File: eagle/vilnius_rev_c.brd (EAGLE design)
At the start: 72 x 42 mm, 43 parts, among them IC1 PIC18F2580, IC3 MCP2551SN, IC4 LM2575S, IC5 MCP604, J1 OSTTE-12, J2 A00-108-220-450, Q1 10 MHz

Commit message: Main functionality in place
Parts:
- moved R107 0.14 mm to (9.67, 30.6)
- moved R102 0.14 mm to (9.64, 13.1)
- moved R101 0.10 mm to (9.61, 9.64)
- moved R103 0.10 mm to (9.61, 16.7)
- moved R105 0.10 mm to (9.62, 23.7)
- moved R100 0.10 mm to (9.59, 6.15)
- moved R104 0.10 mm to (9.59, 20.1)
- moved R106 0.10 mm to (9.68, 27.1)
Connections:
- removed net V+: IC5.4
- removed net V-: IC5.11
- net GND: now also IC5.11
- net VCC: now also IC5.4
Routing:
- net VCC: track 221.6 -> 227.5 mm
- net GND: track 85.9 -> 85.7 mm, vias 8 -> 9
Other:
- board text added: "+5V"
- board text added: "GND"
- board text added: "I/O-0"
- board text added: "I/O-1"
- board text added: "IN0-A"
- board text added: "IN0-B"
- board text added: "IN1-A"
- board text added: "IN1-B"
- board text added: "IN2-A"
- board text added: "IN2-B"
- board text added: "IN3-A"
- board text added: "IN3-B"

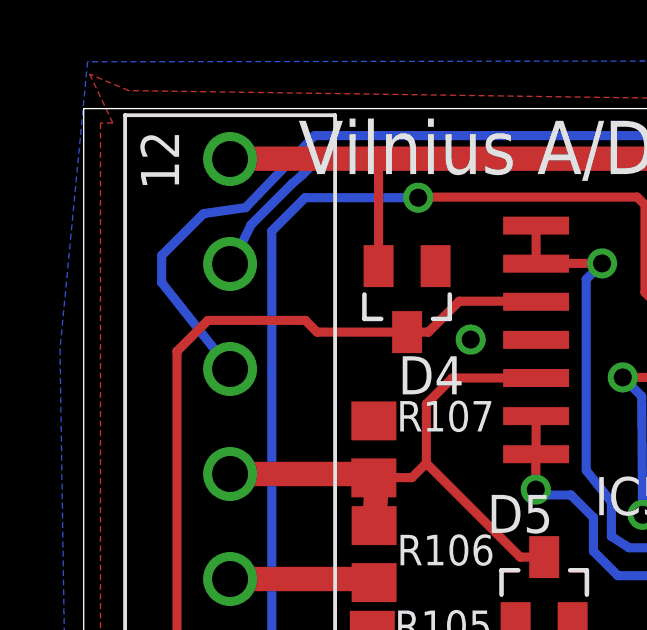
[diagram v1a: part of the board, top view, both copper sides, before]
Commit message: I/O event handling in place
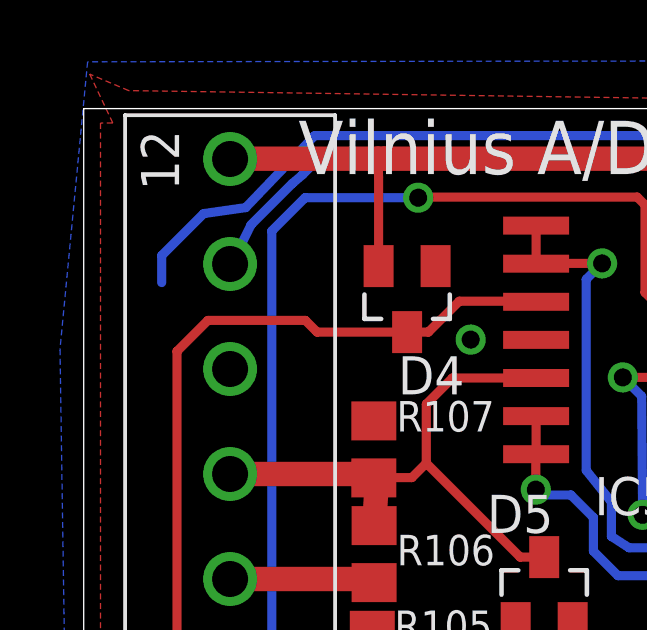
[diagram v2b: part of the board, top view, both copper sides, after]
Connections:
- net IN4-A renamed IO0
- net IN4-B renamed IO1
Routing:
- net IO0: track 40.8 -> 37.1 mm
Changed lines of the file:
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@@
 <wire x1="4.88" y1="12.32" x2="9.64" y2="12.12" width="0.8128" layer="1"/>
-</signal>
-<signal name="IN4-A">
-<contactref element="J1" pad="10"/>
-<contactref element="IC1" pad="16"/>
-<wire x1="4.88" y1="33.32" x2="2.6" y2="36.2" width="0.3048" layer="16"/>
-<wire x1="2.6" y1="36.2" x2="2.6" y2="37.1" width="0.3048" layer="16"/>
-<wire x1="2.6" y1="37.1" x2="4" y2="38.5" width="0.3048" layer="16"/>
-<wire x1="4" y1="38.5" x2="5.4" y2="38.7" width="0.3048" layer="16"/>
-<wire x1="5.4" y1="38.7" x2="7.7" y2="41.1" width="0.3048" layer="16"/>
-<wire x1="7.7" y1="41.1" x2="32.7" y2="41.1" width="0.3048" layer="16"/>
-<wire x1="32.7" y1="41.1" x2="32.9" y2="40.9" width="0.3048" layer="16"/>
-<wire x1="32.9" y1="40.9" x2="32.9" y2="38.9" width="0.3048" layer="16"/>
-<wire x1="32.9" y1="38.9" x2="33.3" y2="38.5" width="0.3048" layer="16"/>
-<via x="33.3" y="38.5" extent="1-16" drill="0.6" shape="square"/>
-<wire x1="33.3" y1="38.5" x2="31.685" y2="38.5" width="0.3048" layer="1"/>
-<wire x1="31.685" y1="38.5" x2="31.66" y2="38.475" width="0.3048" layer="1"/>
-</signal>
-<signal name="IN4-B">
-<contactref element="J1" pad="11"/>
-<contactref element="IC1" pad="15"/>
-<wire x1="30.185" y1="39.745" x2="31.66" y2="39.745" width="0.3048" layer="1"/>
-<wire x1="29.21" y1="39.71" x2="30.185" y2="39.745" width="0.3048" layer="1"/>
-<wire x1="7.92" y1="40.42" x2="27.5" y2="40.5" width="0.3048" layer="16"/>
-<wire x1="27.5" y1="40.5" x2="28" y2="39.71" width="0.3048" layer="16"/>
-<wire x1="28" y1="39.71" x2="29.21" y2="39.71" width="0.3048" layer="16"/>
-<wire x1="7.3" y1="39.8" x2="7.92" y2="40.42" width="0.3048" layer="16"/>
-<wire x1="6.95" y1="39.5" x2="7.3" y2="39.8" width="0.3048" layer="16"/>
-<wire x1="5.58" y1="38.13" x2="6.95" y2="39.5" width="0.3048" layer="16"/>
-<wire x1="4.98" y1="36.92" x2="5.58" y2="38.13" width="0.3048" layer="16"/>
-<wire x1="4.88" y1="36.82" x2="4.98" y2="36.92" width="0.3048" layer="16"/>
-<via x="29.21" y="39.71" extent="1-16" drill="0.6" shape="square"/>
 </signal>
 <signal name="CANL">
@@
 <wire x1="55.38" y1="30.2" x2="55.39" y2="30.19" width="0.4064" layer="1"/>
 </signal>
+<signal name="IO0">
+<contactref element="J1" pad="10"/>
+<contactref element="IC1" pad="16"/>
+<wire x1="2.6" y1="36.2" x2="2.6" y2="37.1" width="0.3048" layer="16"/>
+<wire x1="2.6" y1="37.1" x2="4" y2="38.5" width="0.3048" layer="16"/>
+<wire x1="4" y1="38.5" x2="5.4" y2="38.7" width="0.3048" layer="16"/>
+<wire x1="5.4" y1="38.7" x2="7.7" y2="41.1" width="0.3048" layer="16"/>
+<wire x1="7.7" y1="41.1" x2="32.7" y2="41.1" width="0.3048" layer="16"/>
+<wire x1="32.7" y1="41.1" x2="32.9" y2="40.9" width="0.3048" layer="16"/>
+<wire x1="32.9" y1="40.9" x2="32.9" y2="38.9" width="0.3048" layer="16"/>
+<wire x1="32.9" y1="38.9" x2="33.3" y2="38.5" width="0.3048" layer="16"/>
+<via x="33.3" y="38.5" extent="1-16" drill="0.6" shape="square"/>
+<wire x1="33.3" y1="38.5" x2="31.685" y2="38.5" width="0.3048" layer="1"/>
+<wire x1="31.685" y1="38.5" x2="31.66" y2="38.475" width="0.3048" layer="1"/>
+<wire x1="4.88" y1="33.32" x2="2.6" y2="36.2" width="0" layer="19" extent="16-16"/>
+</signal>
+<signal name="IO1">
+<contactref element="J1" pad="11"/>
+<contactref element="IC1" pad="15"/>
+<wire x1="30.185" y1="39.745" x2="31.66" y2="39.745" width="0.3048" layer="1"/>
+<wire x1="29.21" y1="39.71" x2="30.185" y2="39.745" width="0.3048" layer="1"/>
+<wire x1="7.92" y1="40.42" x2="27.5" y2="40.5" width="0.3048" layer="16"/>
+<wire x1="27.5" y1="40.5" x2="28" y2="39.71" width="0.3048" layer="16"/>
+<wire x1="28" y1="39.71" x2="29.21" y2="39.71" width="0.3048" layer="16"/>
+<wire x1="7.3" y1="39.8" x2="7.92" y2="40.42" width="0.3048" layer="16"/>
+<wire x1="6.95" y1="39.5" x2="7.3" y2="39.8" width="0.3048" layer="16"/>
+<wire x1="5.58" y1="38.13" x2="6.95" y2="39.5" width="0.3048" layer="16"/>
+<wire x1="4.98" y1="36.92" x2="5.58" y2="38.13" width="0.3048" layer="16"/>
+<via x="29.21" y="39.71" extent="1-16" drill="0.6" shape="square"/>
+<wire x1="4.98" y1="36.92" x2="4.88" y2="36.82" width="0" layer="19" extent="16-16"/>
+</signal>
 </signals>

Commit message: Changed value of C14 to 10uF
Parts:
- C8: value 1 uF -> 10 uF
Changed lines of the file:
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@@
 <attribute name="NAME" x="10.428" y="31.236" size="1.016" layer="25" font="fixed"/>
 </element>
-<element name="C8" library="rcl" package="C0805" value="1 uF" x="56.34" y="30.19" smashed="yes" rot="R180">
+<element name="C8" library="rcl" package="C0805" value="10 uF" x="56.34" y="30.19" smashed="yes" rot="R180">
 <attribute name="NAME" x="58.33" y="32.61" size="1.27" layer="25" font="fixed" rot="R180"/>
 </element>
